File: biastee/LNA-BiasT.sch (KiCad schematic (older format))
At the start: 15 parts, among them CON1 DC, P1 ANT, P2 RX, U1 LM317AEMP

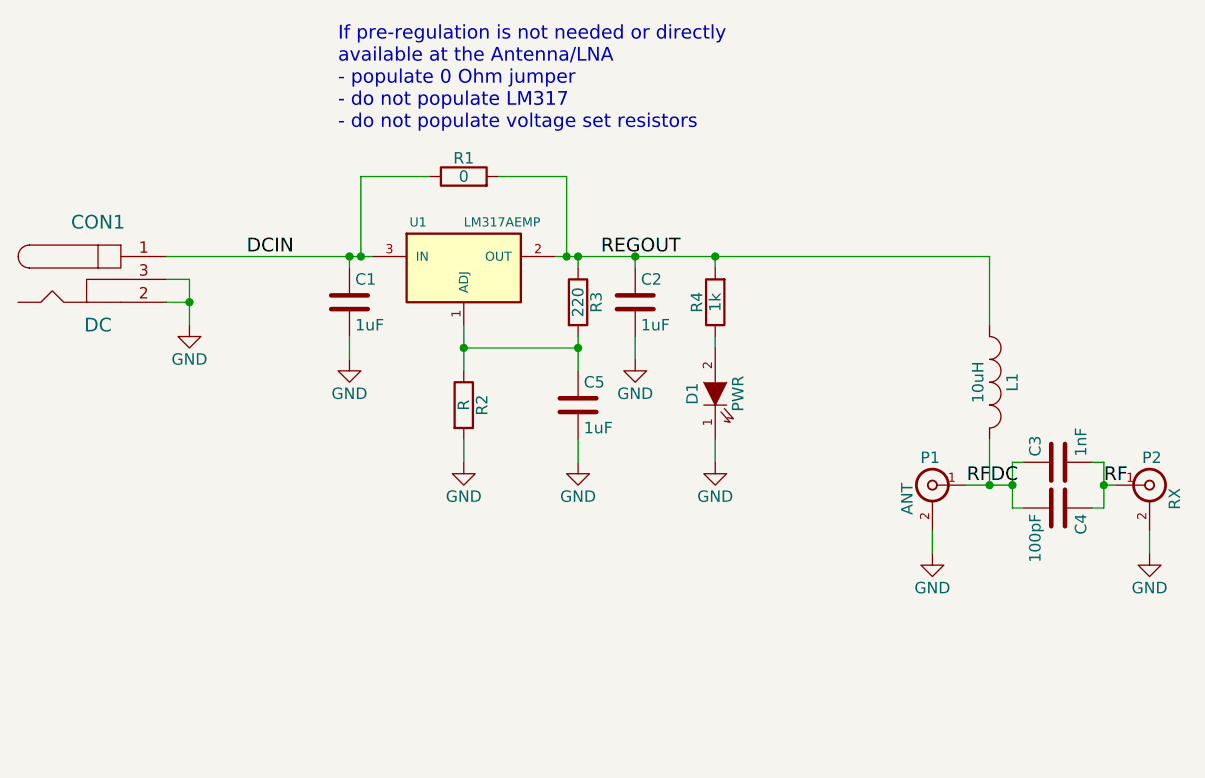
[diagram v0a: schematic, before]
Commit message: added more decoupling capacitors
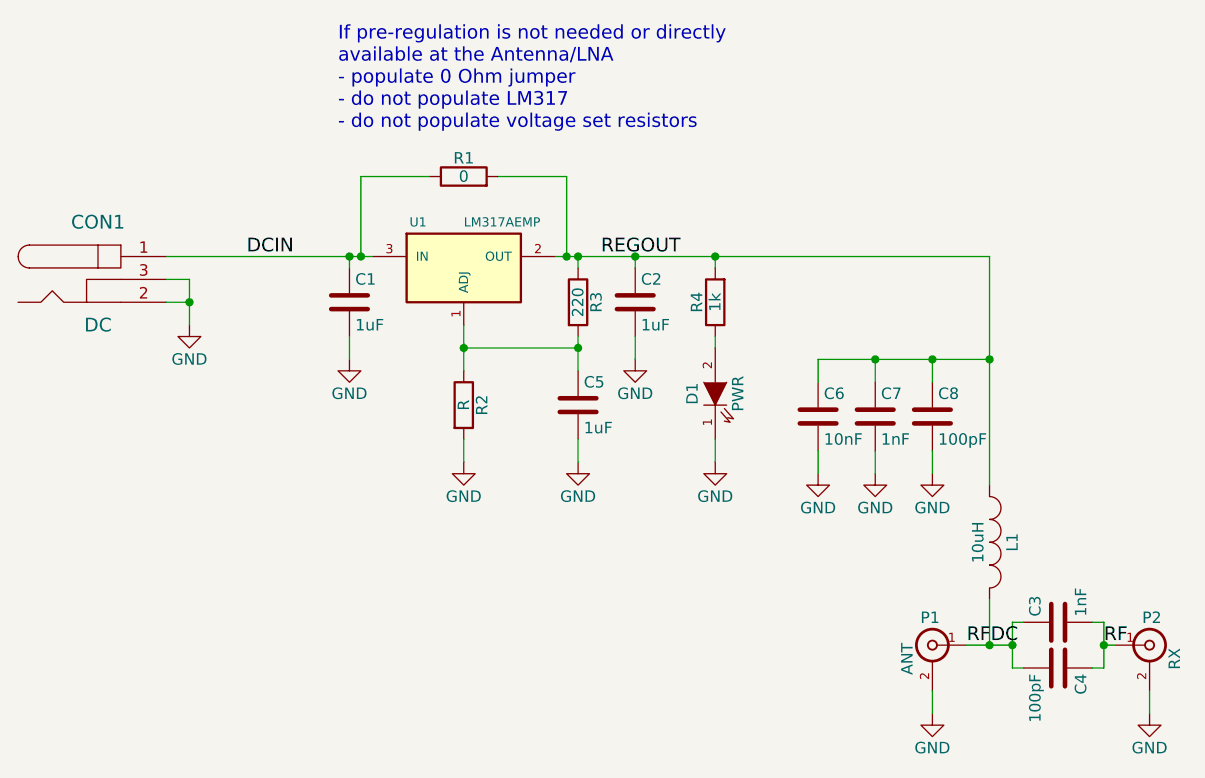
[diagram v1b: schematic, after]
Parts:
- added C6: 10nF, Capacitors_SMD:C_0603_HandSoldering, symbol C
- added C7: 1nF, Capacitors_SMD:C_0603_HandSoldering, symbol C
- added C8: 100pF, Capacitors_SMD:C_0603_HandSoldering, symbol C
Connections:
- net GND: now also C6.2, C7.2, C8.2
- net REGOUT: now also C6.1, C7.1, C8.1
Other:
- moved on the sheet: C3, C4, L1, P1, P2
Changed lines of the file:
@@
 L BNC P1
 U 1 1 555E335B
-P 8250 2900
-F 0 "P1" H 8260 3020 50  0000 C CNN
-F 1 "ANT" V 8360 2840 50  0000 C CNN
-F 2 "devthrash:SMA-BU-P_EdgeMount" H 8250 2900 60  0001 C CNN
-F 3 "" H 8250 2900 60  0000 C CNN
-	1    8250 2900
+P 8250 3600
+F 0 "P1" H 8260 3720 50  0000 C CNN
+F 1 "ANT" V 8360 3540 50  0000 C CNN
+F 2 "devthrash:SMA-BU-P_EdgeMount" H 8250 3600 60  0001 C CNN
+F 3 "" H 8250 3600 60  0000 C CNN
+	1    8250 3600
 	-1   0    0    -1
 $EndComp
@@
 L BNC P2
 U 1 1 555E33D8
-P 9200 2900
-F 0 "P2" H 9210 3020 50  0000 C CNN
-F 1 "RX" V 9310 2840 50  0000 C CNN
-F 2 "devthrash:SMA-BU-P_EdgeMount" H 9200 2900 60  0001 C CNN
-F 3 "" H 9200 2900 60  0000 C CNN
-	1    9200 2900
+P 9200 3600
+F 0 "P2" H 9210 3720 50  0000 C CNN
+F 1 "RX" V 9310 3540 50  0000 C CNN
+F 2 "devthrash:SMA-BU-P_EdgeMount" H 9200 3600 60  0001 C CNN
+F 3 "" H 9200 3600 60  0000 C CNN
+	1    9200 3600
 	1    0    0    -1
 $EndComp
@@
 L C C4
 U 1 1 555E3528
-P 8800 3000
-F 0 "C4" H 8825 3100 50  0000 L CNN
-F 1 "100pF" H 8825 2900 50  0000 L CNN
-F 2 "Capacitors_SMD:C_0603_HandSoldering" H 8838 2850 30  0001 C CNN
-F 3 "" H 8800 3000 60  0000 C CNN
-	1    8800 3000
+P 8800 3700
+F 0 "C4" H 8825 3800 50  0000 L CNN
+F 1 "100pF" H 8825 3600 50  0000 L CNN
+F 2 "Capacitors_SMD:C_0603_HandSoldering" H 8838 3550 30  0001 C CNN
+F 3 "" H 8800 3700 60  0000 C CNN
+	1    8800 3700
 	0    1    1    0
 $EndComp
@@
 L C C3
 U 1 1 555E357F
-P 8800 2800
-F 0 "C3" H 8825 2900 50  0000 L CNN
-F 1 "1nF" H 8825 2700 50  0000 L CNN
-F 2 "Capacitors_SMD:C_0603_HandSoldering" H 8838 2650 30  0001 C CNN
-F 3 "" H 8800 2800 60  0000 C CNN
-	1    8800 2800
+P 8800 3500
+F 0 "C3" H 8825 3600 50  0000 L CNN
+F 1 "1nF" H 8825 3400 50  0000 L CNN
+F 2 "Capacitors_SMD:C_0603_HandSoldering" H 8838 3350 30  0001 C CNN
+F 3 "" H 8800 3500 60  0000 C CNN
+	1    8800 3500
 	0    -1   -1   0
 $EndComp
 Wire Wire Line
-	8600 2800 8600 3000
-Wire Wire Line
-	8600 2800 8650 2800
-Wire Wire Line
-	8400 2900 8600 2900
-Wire Wire Line
-	8600 3000 8650 3000
-Connection ~ 8600 2900
-Wire Wire Line
-	8950 2800 9000 2800
-Wire Wire Line
-	9000 3000 8950 3000
+	8600 3500 8600 3700
+Wire Wire Line
+	8600 3500 8650 3500
+Wire Wire Line
+	8400 3600 8600 3600
+Wire Wire Line
+	8600 3700 8650 3700
+Connection ~ 8600 3600
+Wire Wire Line
+	8950 3500 9000 3500
+Wire Wire Line
+	9000 3700 8950 3700
 $Comp
 L INDUCTOR_SMALL L1
 U 1 1 555E3664
-P 8500 2450
-F 0 "L1" H 8500 2550 50  0000 C CNN
-F 1 "10uH" H 8500 2400 50  0000 C CNN
-F 2 "Resistors_SMD:R_0805_HandSoldering" H 8500 2450 60  0001 C CNN
-F 3 "" H 8500 2450 60  0000 C CNN
-	1    8500 2450
+P 8500 3150
+F 0 "L1" H 8500 3250 50  0000 C CNN
+F 1 "10uH" H 8500 3100 50  0000 C CNN
+F 2 "Resistors_SMD:R_0805_HandSoldering" H 8500 3150 60  0001 C CNN
+F 3 "" H 8500 3150 60  0000 C CNN
+	1    8500 3150
 	0    1    1    0
 $EndComp
 Wire Wire Line
-	8500 2700 8500 2900
-Connection ~ 8500 2900
-$Comp
-L GND #PWR7
+	8500 3400 8500 3600
+Connection ~ 8500 3600
+$Comp
+L GND #PWR01
 U 1 1 555E3706
-P 8250 3200
-F 0 "#PWR7" H 8250 2950 50  0001 C CNN
-F 1 "GND" H 8250 3050 50  0000 C CNN
-F 2 "" H 8250 3200 60  0000 C CNN
-F 3 "" H 8250 3200 60  0000 C CNN
-	1    8250 3200
-	1    0    0    -1
-$EndComp
-$Comp
-L GND #PWR8
+P 8250 3900
+F 0 "#PWR01" H 8250 3650 50  0001 C CNN
+F 1 "GND" H 8250 3750 50  0000 C CNN
+F 2 "" H 8250 3900 60  0000 C CNN
+F 3 "" H 8250 3900 60  0000 C CNN
+	1    8250 3900
+	1    0    0    -1
+$EndComp
+$Comp
+L GND #PWR02
 U 1 1 555E3722
-P 9200 3200
-F 0 "#PWR8" H 9200 2950 50  0001 C CNN
-F 1 "GND" H 9200 3050 50  0000 C CNN
-F 2 "" H 9200 3200 60  0000 C CNN
-F 3 "" H 9200 3200 60  0000 C CNN
-	1    9200 3200
-	1    0    0    -1
-$EndComp
-Wire Wire Line
-	9200 3200 9200 3100
-Wire Wire Line
-	8250 3100 8250 3200
+P 9200 3900
+F 0 "#PWR02" H 9200 3650 50  0001 C CNN
+F 1 "GND" H 9200 3750 50  0000 C CNN
+F 2 "" H 9200 3900 60  0000 C CNN
+F 3 "" H 9200 3900 60  0000 C CNN
+	1    9200 3900
+	1    0    0    -1
+$EndComp
+Wire Wire Line
+	9200 3900 9200 3800
+Wire Wire Line
+	8250 3800 8250 3900
 $Comp
 L LM317AEMP U1
@@
 	6700 1900 6700 1950
 $Comp
-L GND #PWR3
+L GND #PWR03
 U 1 1 555E3BEB
 P 6200 2800
-F 0 "#PWR3" H 6200 2550 50  0001 C CNN
+F 0 "#PWR03" H 6200 2550 50  0001 C CNN
 F 1 "GND" H 6200 2650 50  0000 C CNN
 F 2 "" H 6200 2800 60  0000 C CNN
@@
 $EndComp
 $Comp
-L GND #PWR5
+L GND #PWR04
 U 1 1 555E3C9C
 P 6950 2350
-F 0 "#PWR5" H 6950 2100 50  0001 C CNN
+F 0 "#PWR04" H 6950 2100 50  0001 C CNN
 F 1 "GND" H 6950 2200 50  0000 C CNN
 F 2 "" H 6950 2350 60  0000 C CNN
@@
 $EndComp
 $Comp
-L GND #PWR2
+L GND #PWR05
 U 1 1 555E44FC
 P 5700 2350
-F 0 "#PWR2" H 5700 2100 50  0001 C CNN
+F 0 "#PWR05" H 5700 2100 50  0001 C CNN
 F 1 "GND" H 5700 2200 50  0000 C CNN
 F 2 "" H 5700 2350 60  0000 C CNN
@@
 Connection ~ 5700 1900
 $Comp
-L GND #PWR1
+L GND #PWR06
 U 1 1 555E486E
 P 5000 2200
-F 0 "#PWR1" H 5000 1950 50  0001 C CNN
+F 0 "#PWR06" H 5000 1950 50  0001 C CNN
 F 1 "GND" H 5000 2050 50  0000 C CNN
 F 2 "" H 5000 2200 60  0000 C CNN
@@
 	4900 2100 5000 2100
 Wire Wire Line
-	9000 2800 9000 3000
-Wire Wire Line
-	9050 2900 9000 2900
-Connection ~ 9000 2900
+	9000 3500 9000 3700
+Wire Wire Line
+	9050 3600 9000 3600
+Connection ~ 9000 3600
 Connection ~ 5000 2100
 Wire Wire Line
 	5000 2000 4900 2000
-Text Label 8400 2900 0    60   ~ 0
+Text Label 8400 3600 0    60   ~ 0
 RFDC
-Text Label 9000 2900 0    60   ~ 0
+Text Label 9000 3600 0    60   ~ 0
 RF
 $Comp
@@
 $EndComp
 $Comp
-L GND #PWR4
+L GND #PWR07
 U 1 1 55733FA0
 P 6700 2800
-F 0 "#PWR4" H 6700 2550 50  0001 C CNN
+F 0 "#PWR07" H 6700 2550 50  0001 C CNN
 F 1 "GND" H 6700 2650 50  0000 C CNN
 F 2 "" H 6700 2800 60  0000 C CNN
@@
 	6700 2700 6700 2800
 $Comp
-L GND #PWR6
+L GND #PWR08
 U 1 1 557341D3
 P 7300 2800
-F 0 "#PWR6" H 7300 2550 50  0001 C CNN
+F 0 "#PWR08" H 7300 2550 50  0001 C CNN
 F 1 "GND" H 7300 2650 50  0000 C CNN
 F 2 "" H 7300 2800 60  0000 C CNN
@@
 	7300 2800 7300 2700
 Wire Wire Line
-	8500 1900 8500 2200
+	8500 1900 8500 2900
 Text Label 6800 1900 0    60   ~ 0
 REGOUT
 Text Label 5250 1900 0    60   ~ 0
 DCIN
+$Comp
+L C C8
+U 1 1 557481E1
+P 8250 2600
+F 0 "C8" H 8275 2700 50  0000 L CNN
+F 1 "100pF" H 8275 2500 50  0000 L CNN
+F 2 "Capacitors_SMD:C_0603_HandSoldering" H 8288 2450 30  0001 C CNN
+F 3 "" H 8250 2600 60  0000 C CNN
+	1    8250 2600
+	1    0    0    -1
+$EndComp
+$Comp
+L C C7
+U 1 1 55748232
+P 8000 2600
+F 0 "C7" H 8025 2700 50  0000 L CNN
+F 1 "1nF" H 8025 2500 50  0000 L CNN
+F 2 "Capacitors_SMD:C_0603_HandSoldering" H 8038 2450 30  0001 C CNN
+F 3 "" H 8000 2600 60  0000 C CNN
+	1    8000 2600
+	1    0    0    -1
+$EndComp
+$Comp
+L C C6
+U 1 1 5574826E
+P 7750 2600
+F 0 "C6" H 7775 2700 50  0000 L CNN
+F 1 "10nF" H 7775 2500 50  0000 L CNN
+F 2 "Capacitors_SMD:C_0603_HandSoldering" H 7788 2450 30  0001 C CNN
+F 3 "" H 7750 2600 60  0000 C CNN
+	1    7750 2600
+	1    0    0    -1
+$EndComp
+$Comp
+L GND #PWR09
+U 1 1 55748302
+P 7750 2850
+F 0 "#PWR09" H 7750 2600 50  0001 C CNN
+F 1 "GND" H 7750 2700 50  0000 C CNN
+F 2 "" H 7750 2850 60  0000 C CNN
+F 3 "" H 7750 2850 60  0000 C CNN
+	1    7750 2850
+	1    0    0    -1
+$EndComp
+$Comp
+L GND #PWR010
+U 1 1 55748338
+P 8000 2850
+F 0 "#PWR010" H 8000 2600 50  0001 C CNN
+F 1 "GND" H 8000 2700 50  0000 C CNN
+F 2 "" H 8000 2850 60  0000 C CNN
+F 3 "" H 8000 2850 60  0000 C CNN
+	1    8000 2850
+	1    0    0    -1
+$EndComp
+$Comp
+L GND #PWR011
+U 1 1 55748367
+P 8250 2850
+F 0 "#PWR011" H 8250 2600 50  0001 C CNN
+F 1 "GND" H 8250 2700 50  0000 C CNN
+F 2 "" H 8250 2850 60  0000 C CNN
+F 3 "" H 8250 2850 60  0000 C CNN
+	1    8250 2850
+	1    0    0    -1
+$EndComp
+Wire Wire Line
+	8250 2850 8250 2750
+Wire Wire Line
+	8000 2750 8000 2850
+Wire Wire Line
+	7750 2850 7750 2750
+Wire Wire Line
+	7750 2450 7750 2350
+Wire Wire Line
+	7750 2350 8500 2350
+Connection ~ 8500 2350
+Wire Wire Line
+	8000 2450 8000 2350
+Connection ~ 8000 2350
+Wire Wire Line
+	8250 2450 8250 2350
+Connection ~ 8250 2350
 $EndSCHEMATC
